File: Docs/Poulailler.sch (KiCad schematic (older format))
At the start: 33 parts, among them Q1 Q_PNP_ECB

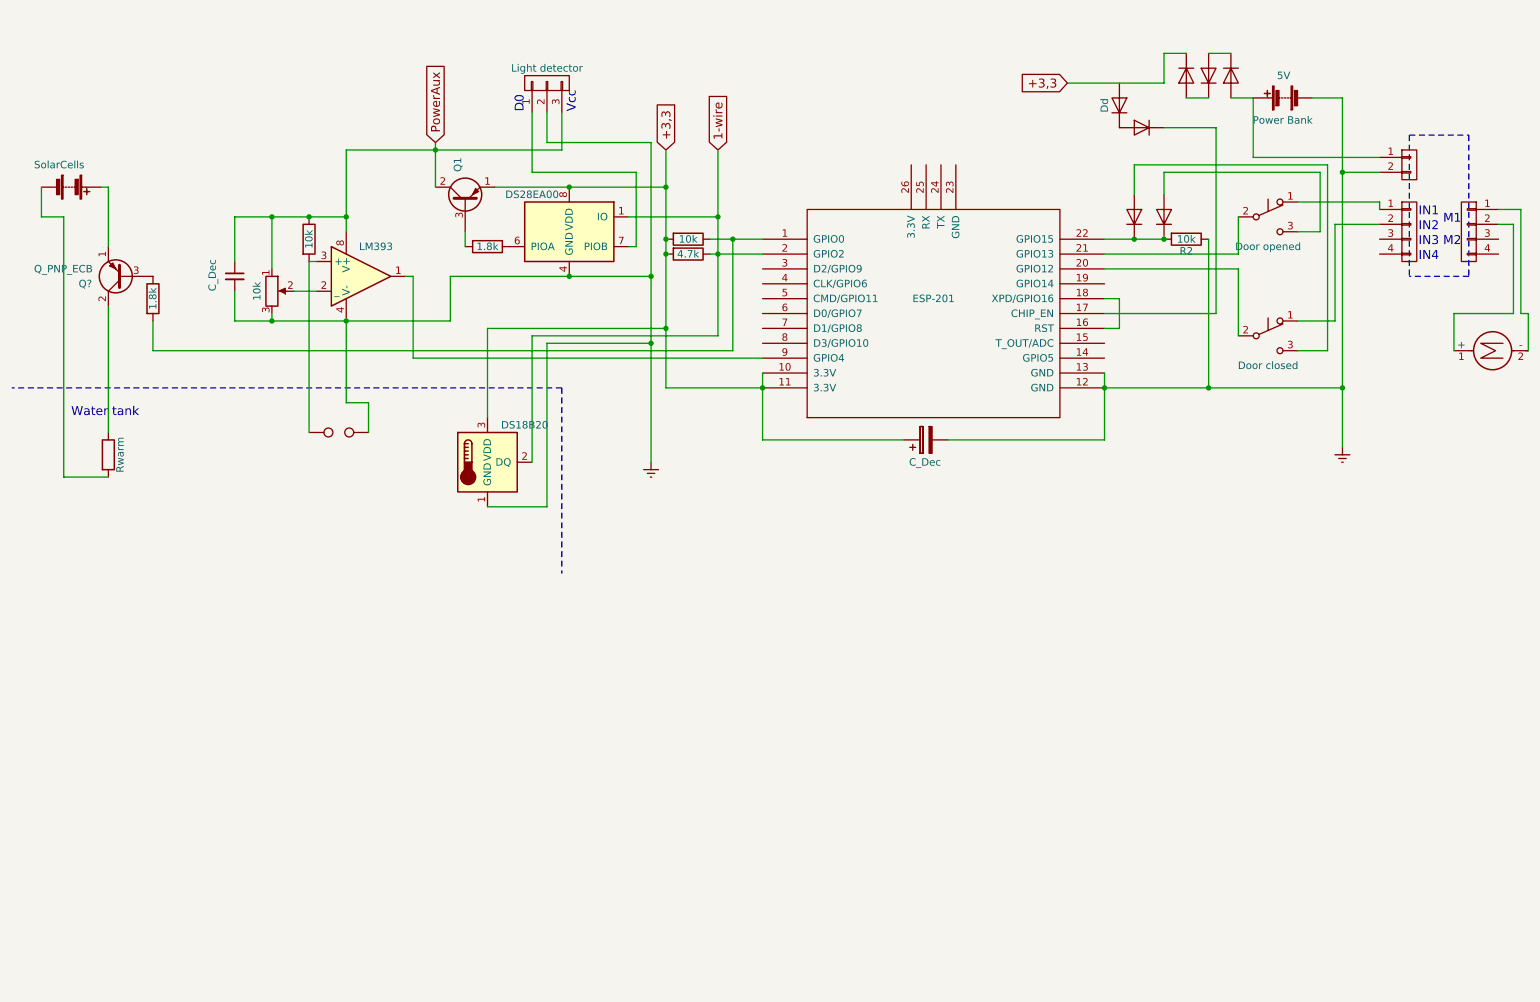
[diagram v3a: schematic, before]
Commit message: Replace DS28EA00 by DHT22
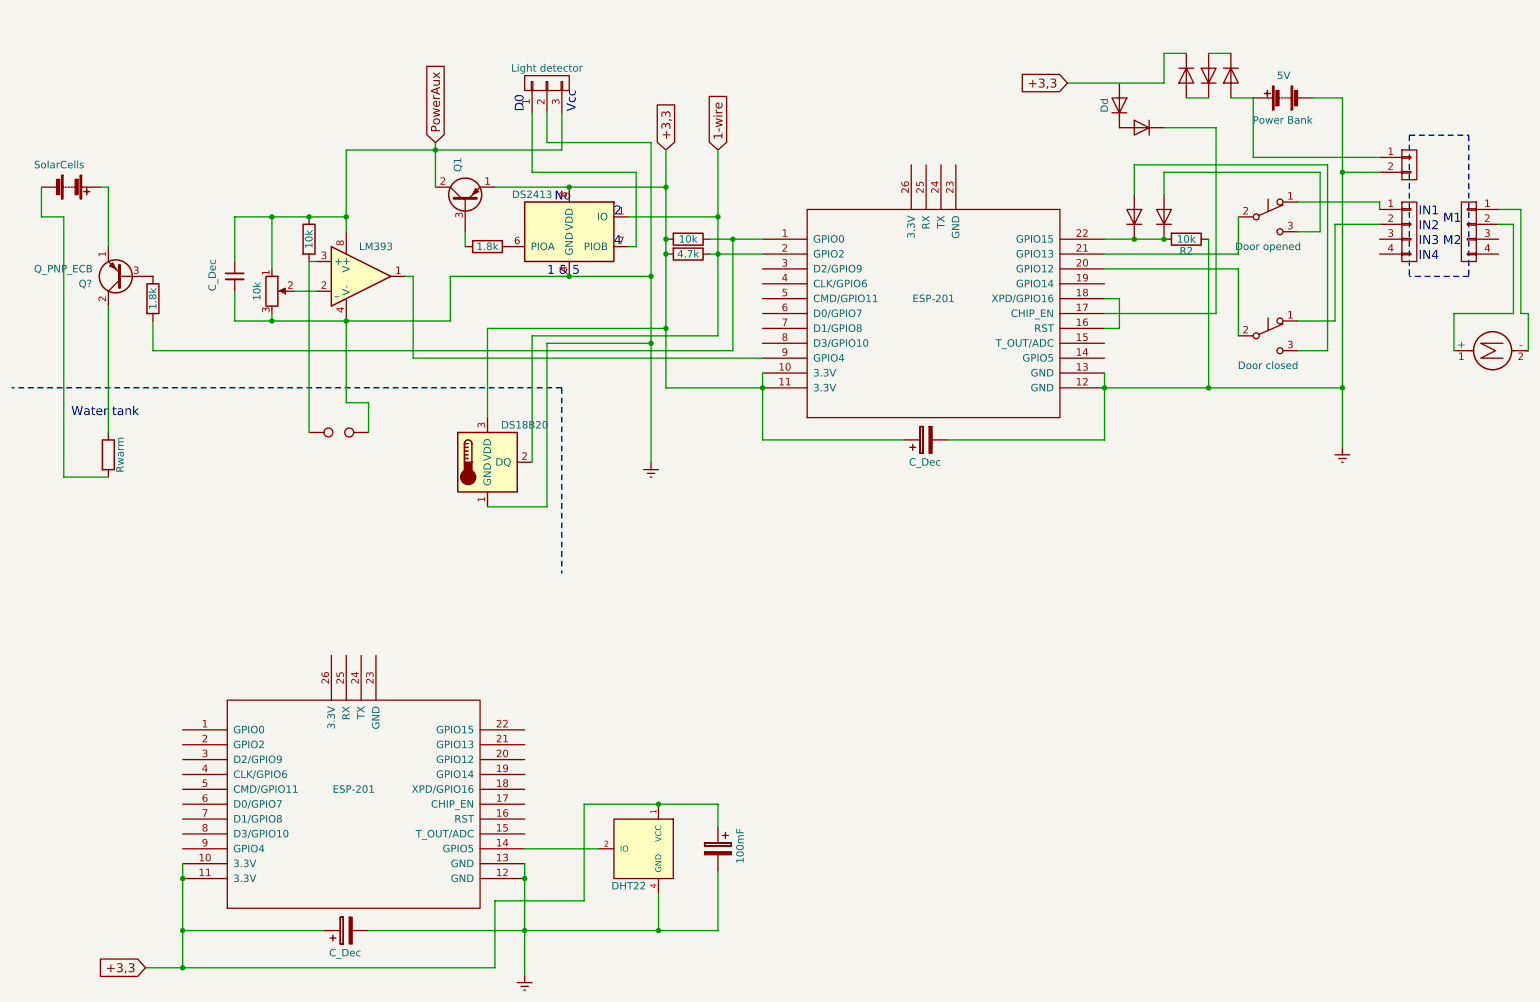
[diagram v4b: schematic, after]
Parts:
- added C?: C_Dec, symbol CP
- added C?: 100mF, symbol CP
- added U?: ESP-201, symbol ESP-201
- added U?: DHT22, symbol DHT11
- U?: value DS28EA00 -> DS2413
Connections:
- net +3,3: now also C?.1, C?.1, U?.1 (VCC), U?.10 (3.3V), U?.11 (3.3V)
- net Earth: now also C?.2, C?.2, U?.12 (GND), U?.13 (GND), U?.4 (GND)
- new net: U?.14 (GPIO5), U?.2 (IO)
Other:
- note added: "1 & 5"
- note added: "2"
- note added: "4"
- note added: "No"
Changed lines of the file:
@@
-$EndComp
-$Comp
-L DS28EA00 U?
-U 1 1 5A233EEF
-P 4400 2000
-F 0 "U?" H 4150 2250 50  0001 C CNN
-F 1 "DS28EA00" H 4650 2250 50  0000 C CNN
-F 2 "Housings_SSOP:MSOP-8_3x3mm_Pitch0.65mm" H 3400 1750 50  0001 C CNN
-F 3 "" H 4150 2250 50  0001 C CNN
-	1    4400 2000
-	-1   0    0    -1
 $EndComp
 $Comp
@@
 Wire Wire Line
 	8750 1300 8750 2550
+$Comp
+L ESP-201 U?
+U 1 1 5A34403E
+P 2950 5850
+F 0 "U?" H 2950 5750 50  0001 C CNN
+F 1 "ESP-201" H 2950 5950 50  0000 C CNN
+F 2 "" H 2950 5850 50  0001 C CNN
+F 3 "" H 2950 5850 50  0001 C CNN
+	1    2950 5850
+	1    0    0    -1
+$EndComp
+$Comp
+L CP C?
+U 1 1 5A344044
+P 2900 6700
+F 0 "C?" H 2925 6800 50  0001 L CNN
+F 1 "C_Dec" V 2750 6600 50  0000 L CNN
+F 2 "" H 2938 6550 50  0001 C CNN
+F 3 "" H 2900 6700 50  0001 C CNN
+	1    2900 6700
+	0    -1   -1   0
+$EndComp
+Wire Wire Line
+	1800 6700 2750 6700
+Wire Wire Line
+	1800 6250 1800 6950
+Connection ~ 1800 6350
+Wire Wire Line
+	4100 6250 4100 7000
+Connection ~ 4100 6350
+$Comp
+L DHT11 U?
+U 1 1 5A344379
+P 4900 6150
+F 0 "U?" H 5050 6400 50  0001 C CNN
+F 1 "DHT22" H 5000 5900 50  0000 C CNN
+F 2 "" H 5050 6400 50  0001 C CNN
+F 3 "" H 5050 6400 50  0001 C CNN
+	1    4900 6150
+	-1   0    0    -1
+$EndComp
+Connection ~ 4100 6700
+$Comp
+L Earth #PWR?
+U 1 1 5A34460B
+P 4100 7000
+F 0 "#PWR?" H 4100 6750 50  0001 C CNN
+F 1 "Earth" H 4100 6850 50  0001 C CNN
+F 2 "" H 4100 7000 50  0001 C CNN
+F 3 "" H 4100 7000 50  0001 C CNN
+	1    4100 7000
+	1    0    0    -1
+$EndComp
+Text GLabel 1550 6950 0    60   Input ~ 0
++3,3
+Wire Wire Line
+	5000 6700 5000 6450
+Wire Wire Line
+	1550 6950 3900 6950
+Connection ~ 1800 6700
+Wire Wire Line
+	3900 6950 3900 6500
+Wire Wire Line
+	4500 6500 4500 5850
+Wire Wire Line
+	4500 5850 5400 5850
+Connection ~ 1800 6950
+$Comp
+L CP C?
+U 1 1 5A344984
+P 5400 6150
+F 0 "C?" H 5425 6250 50  0001 L CNN
+F 1 "100mF" V 5250 6050 50  0000 L CNN
+F 2 "" H 5438 6000 50  0001 C CNN
+F 3 "" H 5400 6150 50  0001 C CNN
+	1    5400 6150
+	-1   0    0    -1
+$EndComp
+Wire Wire Line
+	5400 5850 5400 6000
+Connection ~ 5000 5850
+Wire Wire Line
+	5400 6700 5400 6300
+Connection ~ 5000 6700
+Wire Wire Line
+	4100 6150 4600 6150
+Wire Wire Line
+	3900 6500 4500 6500
+Wire Wire Line
+	3050 6700 5400 6700
+$Comp
+L DS28EA00 U?
+U 1 1 5A233EEF
+P 4400 2000
+F 0 "U?" H 4150 2250 50  0001 C CNN
+F 1 "DS2413" H 4650 2250 50  0000 C CNN
+F 2 "Housings_SSOP:MSOP-8_3x3mm_Pitch0.65mm" H 3400 1750 50  0001 C CNN
+F 3 "" H 4150 2250 50  0001 C CNN
+	1    4400 2000
+	-1   0    0    -1
+$EndComp
+Text Notes 4700 1900 0    60   ~ 0
+2
+Text Notes 4700 2100 0    60   ~ 0
+4
+Text Notes 4250 2300 0    60   ~ 0
+1 & 5
+Text Notes 4300 1800 0    60   ~ 0
+No
 $EndSCHEMATC

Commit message: Missing from last update
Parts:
- removed C?: C_Dec, symbol CP
- removed U?: ESP-201, symbol ESP-201
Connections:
- net +3,3: no longer C?.1, U?.1 (VCC), U?.8 (VDD)
- net at U?.14 (GPIO5): now also U?.2 (IO)
- new net: C?.1, U?.1 (VCC)

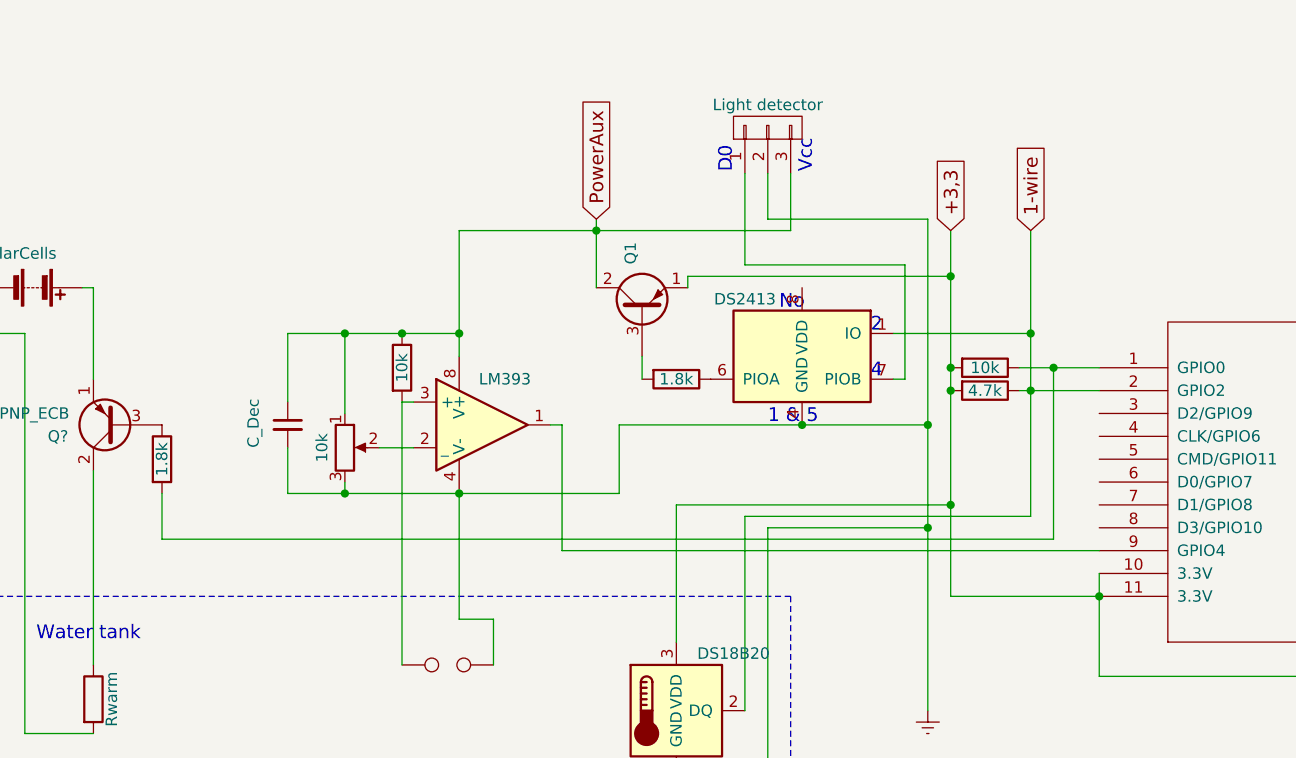
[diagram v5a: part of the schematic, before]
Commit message: GPIO 0 is controling Aux power
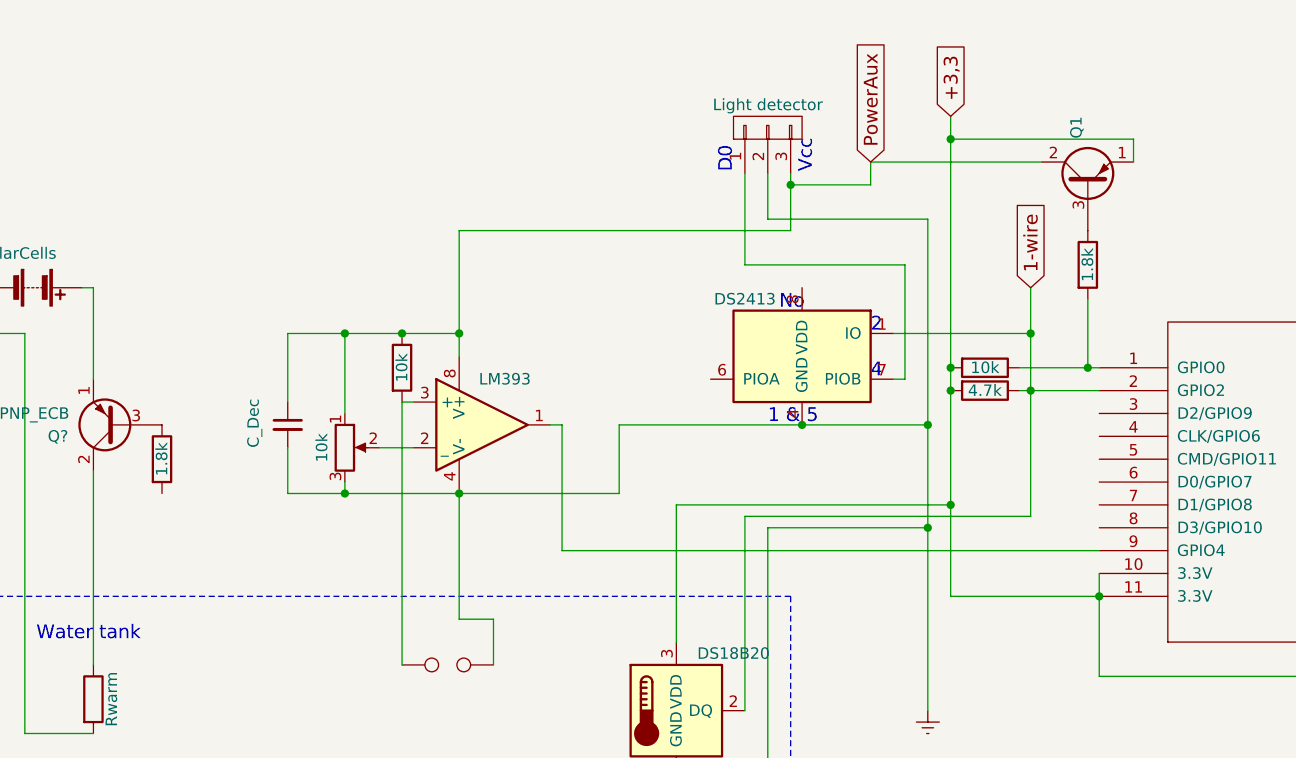
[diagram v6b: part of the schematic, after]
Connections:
- net at R?.1, U?.1 (GPIO0): now also R?.2; no longer R?.2
- net at U?.6 (PIOA): no longer R?.1
- net at Q1.3 (B): now also R?.1; no longer R?.2
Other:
- moved on the sheet: Q1
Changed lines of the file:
@@
 EESchema Schematic File Version 2
-LIBS:maxim
 LIBS:power
 LIBS:transistors
@@
 LIBS:contrib
 LIBS:valves
-LIBS:ESP8266
-LIBS:sensors
-LIBS:device
-LIBS:Switch
-LIBS:Motor
 LIBS:Poulailler-cache
 EELAYER 25 0
@@
 	1    0    0    -1
 $EndComp
-Text GLabel 5050 1450 1    60   Input ~ 0
+Text GLabel 5050 950  1    60   Input ~ 0
 +3,3
 $Comp
@@
 	0    1    1    0
 $EndComp
-Text GLabel 5400 1450 1    60   Input ~ 0
+Text GLabel 5400 1700 1    60   Input ~ 0
 1-wire
 $Comp
@@
 L R R?
 U 1 1 5A234A19
-P 3850 2100
-F 0 "R?" V 3930 2100 50  0001 C CNN
-F 1 "1.8k" V 3850 2100 50  0000 C CNN
-F 2 "" V 3780 2100 50  0000 C CNN
-F 3 "" H 3850 2100 50  0000 C CNN
-	1    3850 2100
-	0    1    1    0
+P 5650 1600
+F 0 "R?" V 5730 1600 50  0001 C CNN
+F 1 "1.8k" V 5650 1600 50  0000 C CNN
+F 2 "" V 5580 1600 50  0000 C CNN
+F 3 "" H 5650 1600 50  0000 C CNN
+	1    5650 1600
+	1    0    0    -1
 $EndComp
 $Comp
 L Q_PNP_ECB Q1
 U 1 1 5A234AEE
-P 3700 1800
-F 0 "Q1" H 4000 1850 50  0000 R CNN
-F 1 "Q_PNP_ECB" H 4300 1750 50  0001 R CNN
-F 2 "" H 3900 1900 50  0000 C CNN
-F 3 "" H 3700 1800 50  0000 C CNN
-	1    3700 1800
+P 5650 1250
+F 0 "Q1" H 5950 1300 50  0000 R CNN
+F 1 "Q_PNP_ECB" H 6250 1200 50  0001 R CNN
+F 2 "" H 5850 1350 50  0000 C CNN
+F 3 "" H 5650 1250 50  0000 C CNN
+	1    5650 1250
 	0    -1   -1   0
 $EndComp
@@
 	0    1    1    0
 $EndComp
-Text GLabel 3500 1400 1    60   Input ~ 0
+Text GLabel 4700 1150 1    60   Input ~ 0
 PowerAux
 $Comp
@@
 Wire Wire Line
 	5350 2150 5700 2150
-Wire Wire Line
-	5050 1450 5050 3050
 Connection ~ 5050 2150
 Connection ~ 5400 2150
@@
 	4950 1400 4950 3550
 Wire Wire Line
-	5400 1450 5400 2700
-Connection ~ 5500 2050
-Wire Wire Line
 	1300 2500 1300 3350
 Connection ~ 5050 2050
 Wire Wire Line
-	3700 2000 3700 2100
-Wire Wire Line
-	3500 1400 3500 1700
-Wire Wire Line
 	4150 1200 4150 1600
 Wire Wire Line
@@
 Wire Wire Line
 	4350 1450 4350 1200
-Connection ~ 3500 1450
 Wire Wire Line
 	3600 2300 4950 2300
@@
 	1000 3650 1300 3650
 Wire Wire Line
-	5500 2800 5500 2050
-Wire Wire Line
 	5400 2700 4150 2700
 Wire Wire Line
@@
 	3850 2650 5050 2650
 Connection ~ 5050 2650
-Wire Wire Line
-	1600 2600 1600 2800
-Wire Wire Line
-	1600 2800 5500 2800
 Wire Notes Line
 	4350 3050 650  3050
@@
 	8750 1300 8750 2550
 Wire Wire Line
-	3900 1700 3900 1650
-Wire Wire Line
-	3900 1650 5050 1650
-Connection ~ 5050 1650
-Wire Wire Line
 	8000 2850 8450 2850
 Wire Wire Line
@@
 Wire Wire Line
 	9100 3350 8850 3350
+Wire Wire Line
+	5400 1700 5400 2700
+Wire Wire Line
+	5050 950  5050 3050
+Wire Wire Line
+	5650 1750 5650 2050
+Connection ~ 5650 2050
+Wire Wire Line
+	5450 1150 4700 1150
+Wire Wire Line
+	4700 1150 4700 1250
+Wire Wire Line
+	4700 1250 4350 1250
+Connection ~ 4350 1250
+Wire Wire Line
+	5050 1050 5850 1050
+Wire Wire Line
+	5850 1050 5850 1150
+Connection ~ 5050 1050
 $EndSCHEMATC

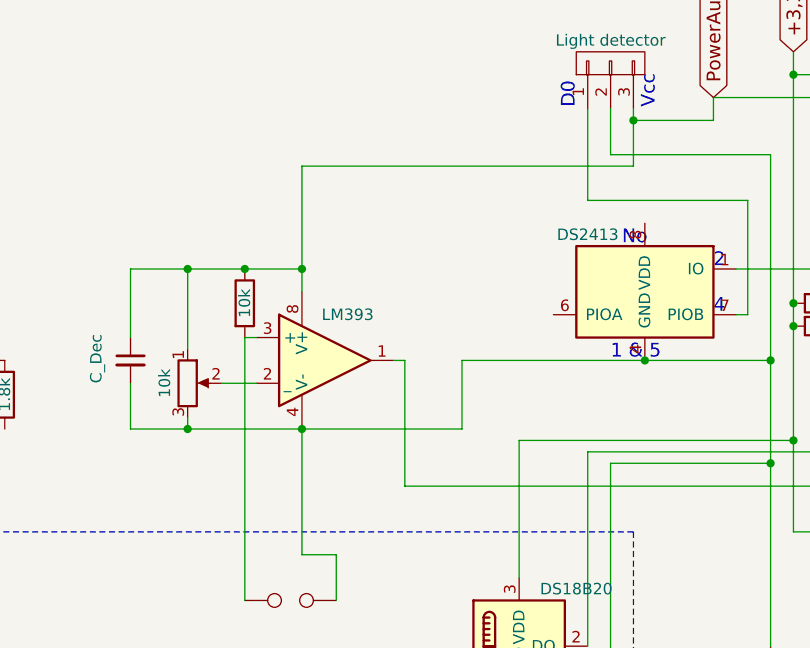
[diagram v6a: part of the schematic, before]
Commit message: Add missing pull-up
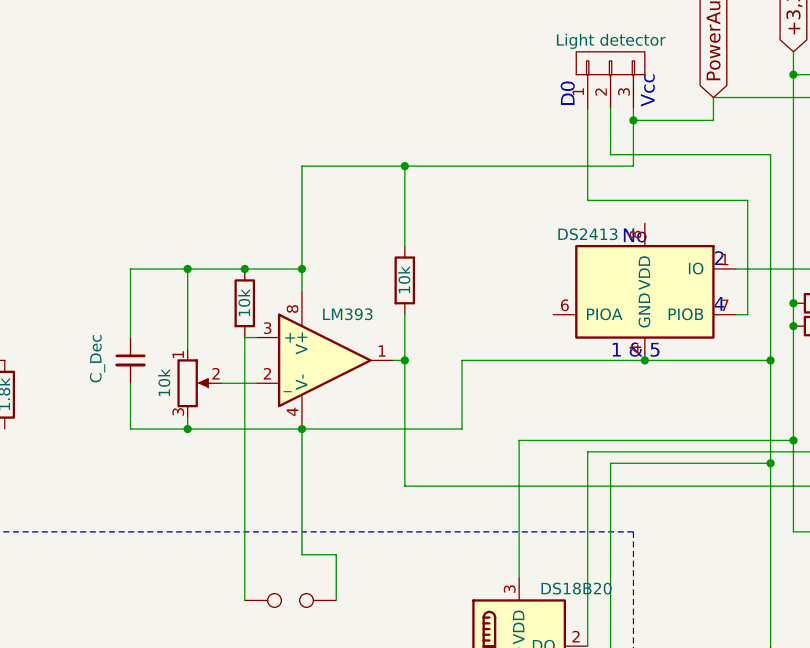
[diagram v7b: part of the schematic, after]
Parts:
- added R?: 10k, symbol R
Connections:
- net PowerAux: now also R?.1
- net at U?.1, U?.9 (GPIO4): now also R?.2
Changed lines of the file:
@@
 	3300 2300 3350 2300
 Wire Wire Line
-	3350 2300 3350 2850
+	3350 2100 3350 2850
 Wire Notes Line
 	4350 3050 4350 4300
@@
 	5850 1050 5850 1150
 Connection ~ 5050 1050
+$Comp
+L R R?
+U 1 1 5A46A837
+P 3350 1950
+F 0 "R?" V 3430 1950 50  0001 C CNN
+F 1 "10k" V 3350 1950 50  0000 C CNN
+F 2 "" V 3280 1950 50  0001 C CNN
+F 3 "" H 3350 1950 50  0001 C CNN
+	1    3350 1950
+	1    0    0    -1
+$EndComp
+Wire Wire Line
+	3350 1450 3350 1800
+Connection ~ 3350 1450
+Connection ~ 3350 2300
 $EndSCHEMATC
